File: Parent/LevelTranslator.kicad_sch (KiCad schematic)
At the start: 9 parts, among them U36 NSL-32, U37 NSL-32, U38 NSL-32

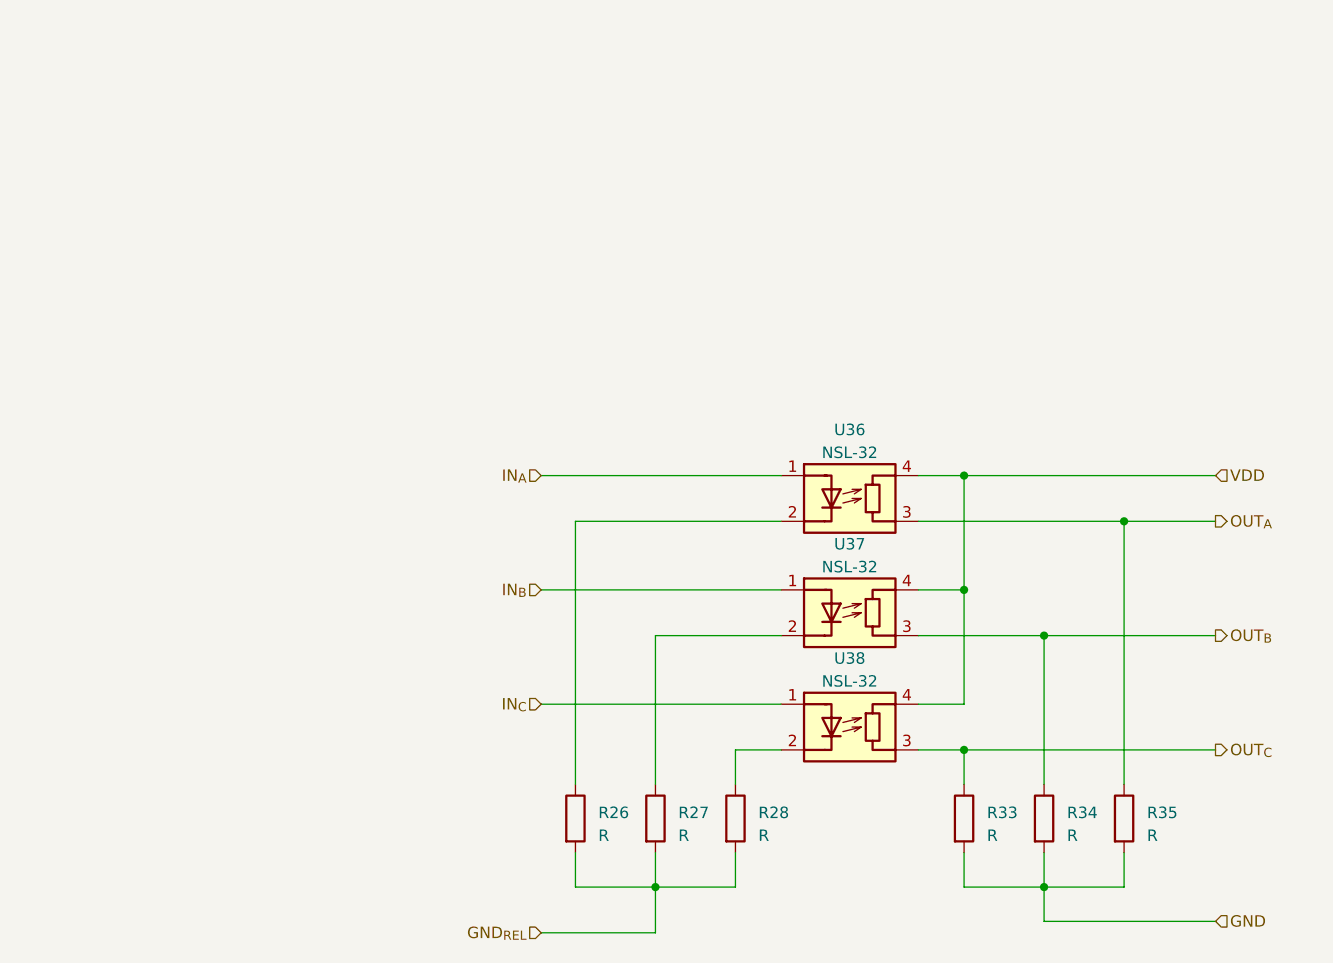
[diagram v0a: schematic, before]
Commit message: Updated Parent further - Move workspace to cloud
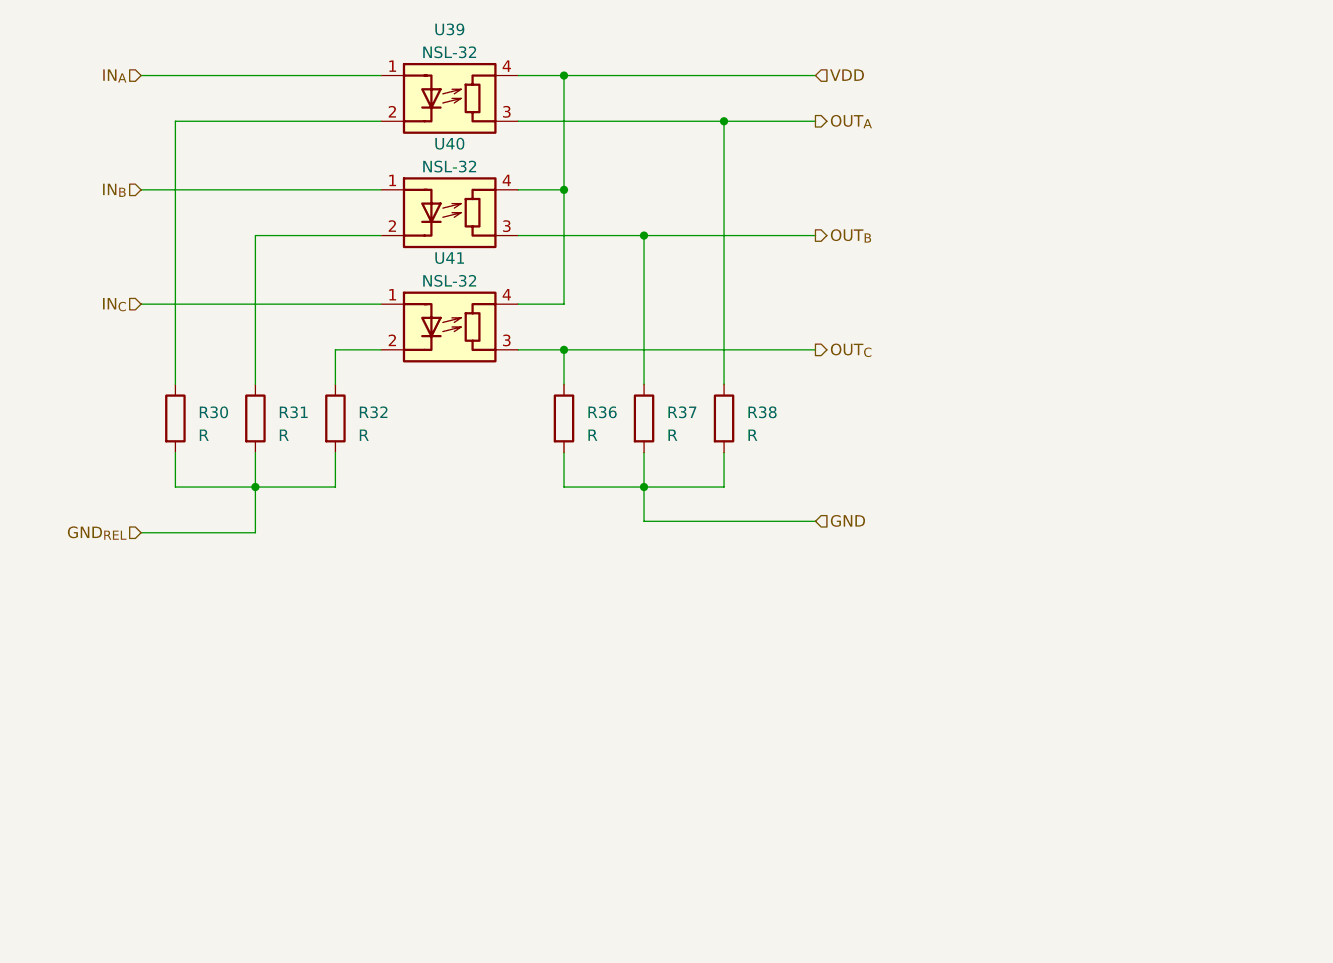
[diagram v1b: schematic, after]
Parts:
- renumbered R26 to R30, R27 to R31, R28 to R32, R33 to R36, R34 to R37, R35 to R38, U36 to U39, U37 to U40, U38 to U41
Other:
- moved on the sheet: R30, R31, R32, R36, R37, R38, U39, U40, U41

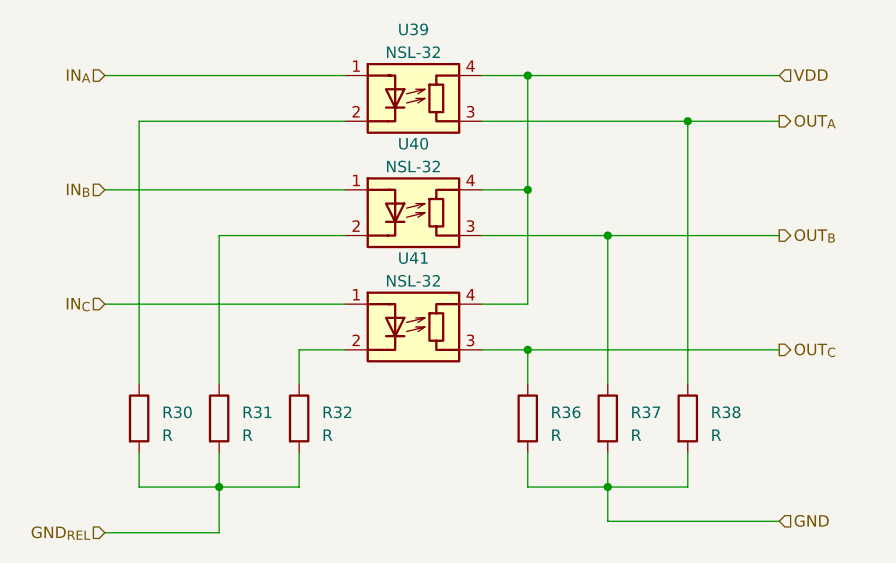
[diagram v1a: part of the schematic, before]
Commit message: Updated Parent further - Move workspace to cloud
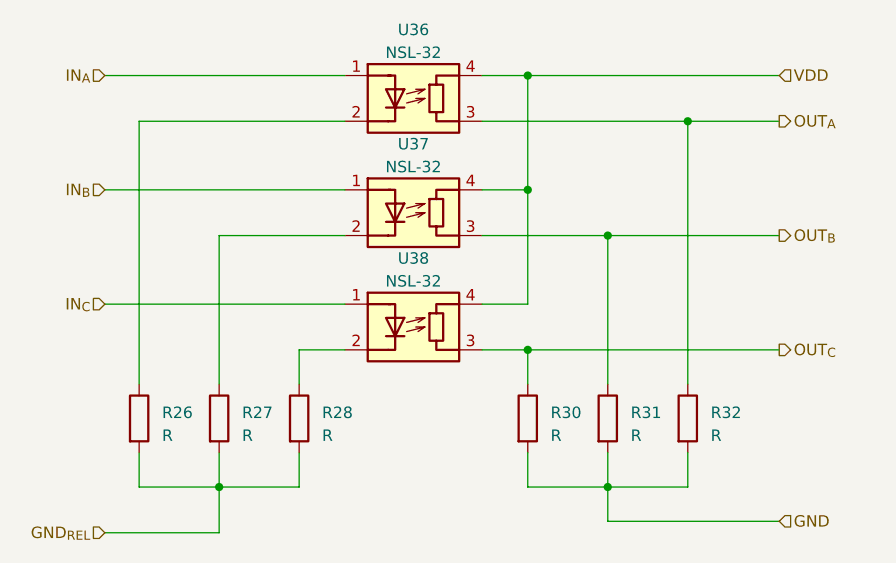
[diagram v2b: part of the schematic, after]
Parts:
- renumbered R30 to R26, R31 to R27, R32 to R28, R36 to R30, R37 to R31, R38 to R32, U39 to U36, U40 to U37, U41 to U38
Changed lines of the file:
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@@
   (symbol (lib_id "Device:R") (at 44.45 57.15 0) (unit 1)
     (in_bom yes) (on_board yes) (dnp no) (fields_autoplaced)
-    (property "Reference" "R32" (at 46.99 56.515 0)
+    (property "Reference" "R28" (at 46.99 56.515 0)
       (effects (font (size 1.27 1.27)) (justify left))
     )
@@
   (symbol (lib_id "Isolator:NSL-32") (at 57.15 21.59 0) (unit 1)
     (in_bom yes) (on_board yes) (dnp no) (fields_autoplaced)
-    (property "Reference" "U39" (at 57.15 13.97 0)
+    (property "Reference" "U36" (at 57.15 13.97 0)
       (effects (font (size 1.27 1.27)))
     )
@@
   (symbol (lib_id "Isolator:NSL-32") (at 57.15 34.29 0) (unit 1)
     (in_bom yes) (on_board yes) (dnp no) (fields_autoplaced)
-    (property "Reference" "U40" (at 57.15 26.67 0)
+    (property "Reference" "U37" (at 57.15 26.67 0)
       (effects (font (size 1.27 1.27)))
     )
@@
   (symbol (lib_id "Device:R") (at 87.63 57.15 0) (unit 1)
     (in_bom yes) (on_board yes) (dnp no) (fields_autoplaced)
-    (property "Reference" "R38" (at 90.17 56.515 0)
+    (property "Reference" "R32" (at 90.17 56.515 0)
       (effects (font (size 1.27 1.27)) (justify left))
     )
@@
   (symbol (lib_id "Device:R") (at 78.74 57.15 0) (unit 1)
     (in_bom yes) (on_board yes) (dnp no) (fields_autoplaced)
-    (property "Reference" "R37" (at 81.28 56.515 0)
+    (property "Reference" "R31" (at 81.28 56.515 0)
       (effects (font (size 1.27 1.27)) (justify left))
     )
@@
   (symbol (lib_id "Device:R") (at 26.67 57.15 0) (unit 1)
     (in_bom yes) (on_board yes) (dnp no) (fields_autoplaced)
-    (property "Reference" "R30" (at 29.21 56.515 0)
+    (property "Reference" "R26" (at 29.21 56.515 0)
       (effects (font (size 1.27 1.27)) (justify left))
     )
@@
   (symbol (lib_id "Device:R") (at 35.56 57.15 0) (unit 1)
     (in_bom yes) (on_board yes) (dnp no) (fields_autoplaced)
-    (property "Reference" "R31" (at 38.1 56.515 0)
+    (property "Reference" "R27" (at 38.1 56.515 0)
       (effects (font (size 1.27 1.27)) (justify left))
     )
@@
   (symbol (lib_id "Device:R") (at 69.85 57.15 0) (unit 1)
     (in_bom yes) (on_board yes) (dnp no) (fields_autoplaced)
-    (property "Reference" "R36" (at 72.39 56.515 0)
+    (property "Reference" "R30" (at 72.39 56.515 0)
       (effects (font (size 1.27 1.27)) (justify left))
     )
@@
   (symbol (lib_id "Isolator:NSL-32") (at 57.15 46.99 0) (unit 1)
     (in_bom yes) (on_board yes) (dnp no) (fields_autoplaced)
-    (property "Reference" "U41" (at 57.15 39.37 0)
-      (effects (font (size 1.27 1.27)))
-    )
+    (property "Reference" "U38" (at 57.15 39.37 0)
+      (effects (font (size 1.27 1.27)))
+    )
